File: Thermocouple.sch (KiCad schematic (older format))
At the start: 23 parts, among them P2 CONN_2, P3 CONN_3X2, U10 LMT84, U11 OPA4170, U9 MCP3901

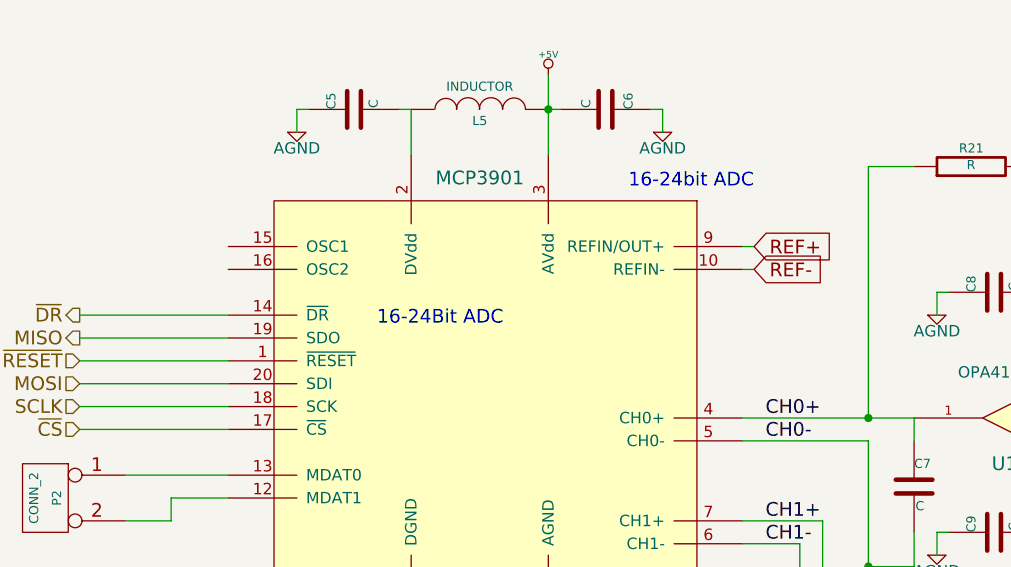
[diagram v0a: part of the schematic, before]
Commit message: Connected remaining ADC pins, some silk screen updates
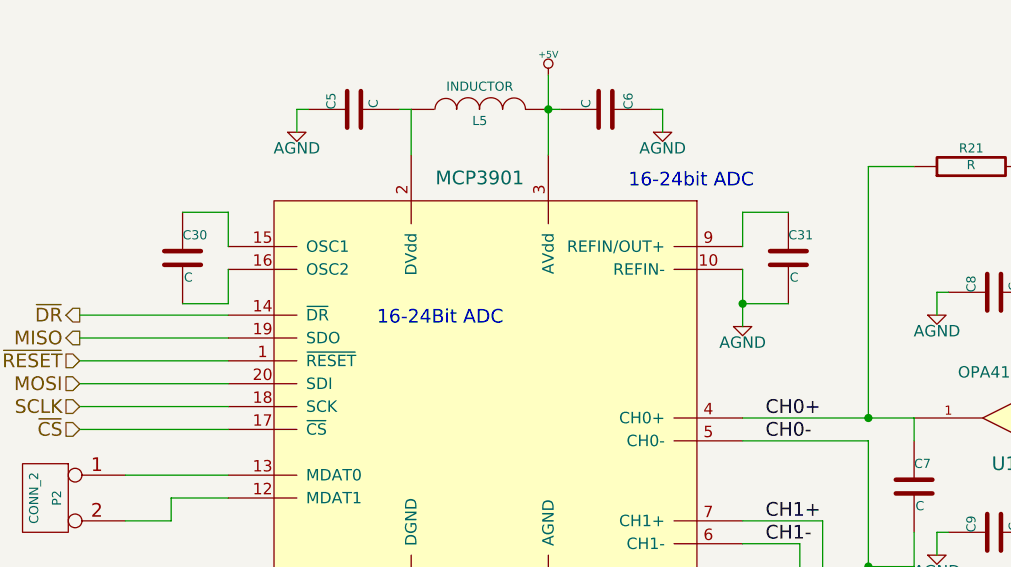
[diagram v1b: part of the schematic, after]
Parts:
- added C30, C31: C, symbol C
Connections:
- net REF- is gone; now on net AGND: U9.10 (REFIN-)
- net AGND: now also C31.2
- net at U9.15 (OSC1): now also C30.1
- net at U9.16 (OSC2): now also C30.2
- net REF+: no longer names the net of U9.9 (REFIN/OUT+)
- net REF+: now also C31.1
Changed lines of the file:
@@
 $EndComp
 $Comp
-L +5V #PWR60
+L +5V #PWR045
 U 1 1 530546E7
 P 5050 4750
-F 0 "#PWR60" H 5050 4840 20  0001 C CNN
+F 0 "#PWR045" H 5050 4840 20  0001 C CNN
 F 1 "+5V" H 5050 4840 30  0000 C CNN
 F 2 "" H 5050 4750 60  0000 C CNN
@@
 $EndComp
 $Comp
-L +5V #PWR53
+L +5V #PWR046
 U 1 1 53054B2C
 P 3100 1500
-F 0 "#PWR53" H 3100 1590 20  0001 C CNN
+F 0 "#PWR046" H 3100 1590 20  0001 C CNN
 F 1 "+5V" H 3100 1590 30  0000 C CNN
 F 2 "" H 3100 1500 60  0000 C CNN
@@
 	1    0    0    -1
 $EndComp
-Text GLabel 4000 2250 2    60   Input ~ 0
-REF+
-Text GLabel 4000 2350 2    60   Input ~ 0
-REF-
 $Comp
 L C C6
@@
 	3600 1650 3600 1750
 Wire Wire Line
-	4000 2350 3950 2350
-Wire Wire Line
-	4000 2250 3950 2250
-Wire Wire Line
 	3100 1500 3100 1850
 Connection ~ 5300 3500
@@
 	1050 3050 1700 3050
 $Comp
-L FE_V+ #PWR66
+L FE_V+ #PWR047
 U 1 1 530BD56D
 P 7800 4750
-F 0 "#PWR66" H 7800 4850 30  0001 C CNN
+F 0 "#PWR047" H 7800 4850 30  0001 C CNN
 F 1 "FE_V+" H 7800 4850 30  0000 C CNN
 F 2 "" H 7800 4750 60  0000 C CNN
@@
 $EndComp
 $Comp
-L FE_V+ #PWR62
+L FE_V+ #PWR048
 U 1 1 530BD573
 P 5300 3550
-F 0 "#PWR62" H 5300 3650 30  0001 C CNN
+F 0 "#PWR048" H 5300 3650 30  0001 C CNN
 F 1 "FE_V+" H 5300 3650 30  0000 C CNN
 F 2 "" H 5300 3550 60  0000 C CNN
@@
 $EndComp
 $Comp
-L FE_V+ #PWR63
+L FE_V+ #PWR049
 U 1 1 530BD635
 P 7800 1400
-F 0 "#PWR63" H 7800 1500 30  0001 C CNN
+F 0 "#PWR049" H 7800 1500 30  0001 C CNN
 F 1 "FE_V+" H 7800 1500 30  0000 C CNN
 F 2 "" H 7800 1400 60  0000 C CNN
@@
 Connection ~ 4200 6300
 $Comp
-L AGND #PWR51
+L AGND #PWR050
 U 1 1 531630FA
 P 2000 1750
-F 0 "#PWR51" H 2000 1750 40  0001 C CNN
+F 0 "#PWR050" H 2000 1750 40  0001 C CNN
 F 1 "AGND" H 2000 1680 50  0000 C CNN
 F 2 "" H 2000 1750 60  0000 C CNN
@@
 $EndComp
 $Comp
-L AGND #PWR55
+L AGND #PWR051
 U 1 1 53163116
 P 3600 1750
-F 0 "#PWR55" H 3600 1750 40  0001 C CNN
+F 0 "#PWR051" H 3600 1750 40  0001 C CNN
 F 1 "AGND" H 3600 1680 50  0000 C CNN
 F 2 "" H 3600 1750 60  0000 C CNN
@@
 $EndComp
 $Comp
-L AGND #PWR52
+L AGND #PWR052
 U 1 1 5316312B
 P 2500 4050
-F 0 "#PWR52" H 2500 4050 40  0001 C CNN
+F 0 "#PWR052" H 2500 4050 40  0001 C CNN
 F 1 "AGND" H 2500 3980 50  0000 C CNN
 F 2 "" H 2500 4050 60  0000 C CNN
@@
 $EndComp
 $Comp
-L AGND #PWR54
+L AGND #PWR053
 U 1 1 53163136
 P 3100 4050
-F 0 "#PWR54" H 3100 4050 40  0001 C CNN
+F 0 "#PWR053" H 3100 4050 40  0001 C CNN
 F 1 "AGND" H 3100 3980 50  0000 C CNN
 F 2 "" H 3100 4050 60  0000 C CNN
@@
 $EndComp
 $Comp
-L AGND #PWR56
+L AGND #PWR054
 U 1 1 53163155
 P 4200 6450
-F 0 "#PWR56" H 4200 6450 40  0001 C CNN
+F 0 "#PWR054" H 4200 6450 40  0001 C CNN
 F 1 "AGND" H 4200 6380 50  0000 C CNN
 F 2 "" H 4200 6450 60  0000 C CNN
@@
 $EndComp
 $Comp
-L AGND #PWR58
+L AGND #PWR055
 U 1 1 5316316A
 P 4800 2550
-F 0 "#PWR58" H 4800 2550 40  0001 C CNN
+F 0 "#PWR055" H 4800 2550 40  0001 C CNN
 F 1 "AGND" H 4800 2480 50  0000 C CNN
 F 2 "" H 4800 2550 60  0000 C CNN
@@
 $EndComp
 $Comp
-L AGND #PWR59
+L AGND #PWR056
 U 1 1 53163175
 P 4800 3600
-F 0 "#PWR59" H 4800 3600 40  0001 C CNN
+F 0 "#PWR056" H 4800 3600 40  0001 C CNN
 F 1 "AGND" H 4800 3530 50  0000 C CNN
 F 2 "" H 4800 3600 60  0000 C CNN
@@
 $EndComp
 $Comp
-L AGND #PWR57
+L AGND #PWR057
 U 1 1 531E51B9
 P 4500 4450
-F 0 "#PWR57" H 4500 4450 40  0001 C CNN
+F 0 "#PWR057" H 4500 4450 40  0001 C CNN
 F 1 "AGND" H 4500 4380 50  0000 C CNN
 F 2 "" H 4500 4450 60  0000 C CNN
@@
 Wire Wire Line
 	2500 1650 2500 1850
+$Comp
+L C C30
+U 1 1 5320C63A
+P 1500 2300
+F 0 "C30" H 1500 2400 40  0000 L CNN
+F 1 "C" H 1506 2215 40  0000 L CNN
+F 2 "" H 1538 2150 30  0000 C CNN
+F 3 "" H 1500 2300 60  0000 C CNN
+	1    1500 2300
+	1    0    0    -1
+$EndComp
+Wire Wire Line
+	1500 2100 1700 2100
+Wire Wire Line
+	1700 2100 1700 2250
+Wire Wire Line
+	1500 2500 1700 2500
+Wire Wire Line
+	1700 2500 1700 2350
+$Comp
+L C C31
+U 1 1 5320C72E
+P 4150 2300
+F 0 "C31" H 4150 2400 40  0000 L CNN
+F 1 "C" H 4156 2215 40  0000 L CNN
+F 2 "" H 4188 2150 30  0000 C CNN
+F 3 "" H 4150 2300 60  0000 C CNN
+	1    4150 2300
+	1    0    0    -1
+$EndComp
+Wire Wire Line
+	4150 2100 3950 2100
+Wire Wire Line
+	4150 2500 3950 2500
+Wire Wire Line
+	3950 2100 3950 2250
+Wire Wire Line
+	3950 2350 3950 2600
+$Comp
+L AGND #PWR058
+U 1 1 5320CB7D
+P 3950 2600
+F 0 "#PWR058" H 3950 2600 40  0001 C CNN
+F 1 "AGND" H 3950 2530 50  0000 C CNN
+F 2 "" H 3950 2600 60  0000 C CNN
+F 3 "" H 3950 2600 60  0000 C CNN
+	1    3950 2600
+	1    0    0    -1
+$EndComp
+Connection ~ 3950 2500
 $EndSCHEMATC

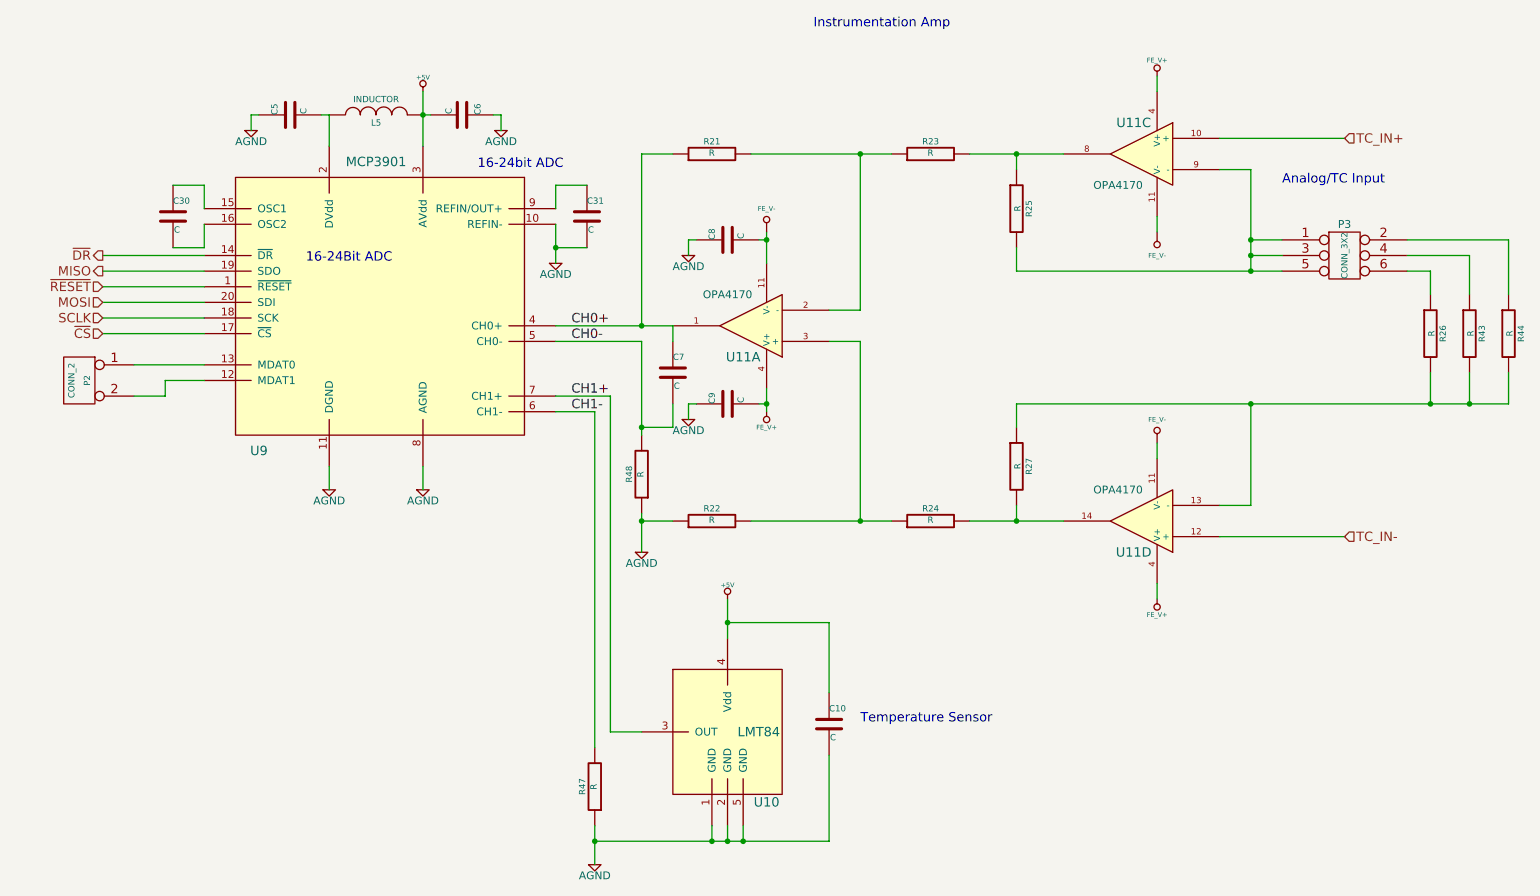
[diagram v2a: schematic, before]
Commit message: Test points added, silk screen updates
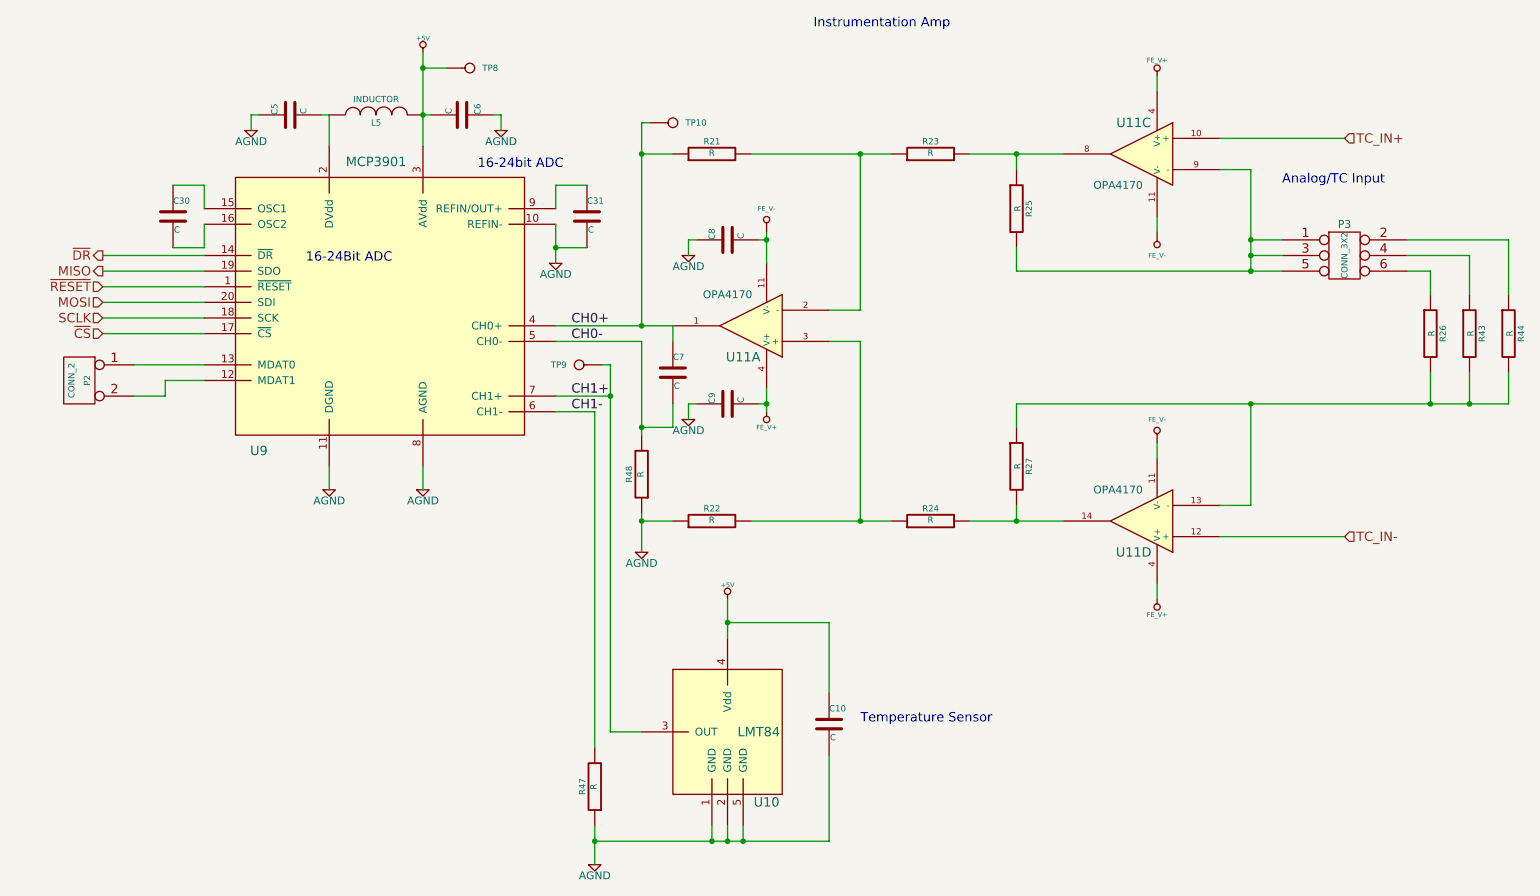
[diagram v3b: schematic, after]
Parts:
- added TP10: CH0+, symbol CONN_1
- added TP8: +5V, symbol CONN_1
- added TP9: CH1+, symbol CONN_1
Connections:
- net +5V: now also TP8.1
- net CH0+: now also TP10.1
- net CH1+: now also TP9.1
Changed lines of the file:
@@
 $EndComp
 $Comp
-L +5V #PWR63
+L +5V #PWR047
 U 1 1 530546E7
 P 5050 4750
-F 0 "#PWR63" H 5050 4840 20  0001 C CNN
+F 0 "#PWR047" H 5050 4840 20  0001 C CNN
 F 1 "+5V" H 5050 4840 30  0000 C CNN
 F 2 "" H 5050 4750 60  0000 C CNN
@@
 $EndComp
 $Comp
-L +5V #PWR55
+L +5V #PWR048
 U 1 1 53054B2C
-P 3100 1500
-F 0 "#PWR55" H 3100 1590 20  0001 C CNN
-F 1 "+5V" H 3100 1590 30  0000 C CNN
-F 2 "" H 3100 1500 60  0000 C CNN
-F 3 "" H 3100 1500 60  0000 C CNN
-	1    3100 1500
+P 3100 1250
+F 0 "#PWR048" H 3100 1340 20  0001 C CNN
+F 1 "+5V" H 3100 1340 30  0000 C CNN
+F 2 "" H 3100 1250 60  0000 C CNN
+F 3 "" H 3100 1250 60  0000 C CNN
+	1    3100 1250
 	1    0    0    -1
 $EndComp
@@
 $EndComp
 $Comp
-L FE_V+ #PWR69
+L FE_V+ #PWR049
 U 1 1 530BD56D
 P 7800 4750
-F 0 "#PWR69" H 7800 4850 30  0001 C CNN
+F 0 "#PWR049" H 7800 4850 30  0001 C CNN
 F 1 "FE_V+" H 7800 4850 30  0000 C CNN
 F 2 "" H 7800 4750 60  0000 C CNN
@@
 $EndComp
 $Comp
-L FE_V+ #PWR65
+L FE_V+ #PWR050
 U 1 1 530BD573
 P 5300 3550
-F 0 "#PWR65" H 5300 3650 30  0001 C CNN
+F 0 "#PWR050" H 5300 3650 30  0001 C CNN
 F 1 "FE_V+" H 5300 3650 30  0000 C CNN
 F 2 "" H 5300 3550 60  0000 C CNN
@@
 $EndComp
 $Comp
-L FE_V+ #PWR66
+L FE_V+ #PWR051
 U 1 1 530BD635
 P 7800 1400
-F 0 "#PWR66" H 7800 1500 30  0001 C CNN
+F 0 "#PWR051" H 7800 1500 30  0001 C CNN
 F 1 "FE_V+" H 7800 1500 30  0000 C CNN
 F 2 "" H 7800 1400 60  0000 C CNN
@@
 $EndComp
 $Comp
-L AGND #PWR53
+L AGND #PWR052
 U 1 1 531630FA
 P 2000 1750
-F 0 "#PWR53" H 2000 1750 40  0001 C CNN
+F 0 "#PWR052" H 2000 1750 40  0001 C CNN
 F 1 "AGND" H 2000 1680 50  0000 C CNN
 F 2 "" H 2000 1750 60  0000 C CNN
@@
 $EndComp
 $Comp
-L AGND #PWR57
+L AGND #PWR053
 U 1 1 53163116
 P 3600 1750
-F 0 "#PWR57" H 3600 1750 40  0001 C CNN
+F 0 "#PWR053" H 3600 1750 40  0001 C CNN
 F 1 "AGND" H 3600 1680 50  0000 C CNN
 F 2 "" H 3600 1750 60  0000 C CNN
@@
 $EndComp
 $Comp
-L AGND #PWR54
+L AGND #PWR054
 U 1 1 5316312B
 P 2500 4050
-F 0 "#PWR54" H 2500 4050 40  0001 C CNN
+F 0 "#PWR054" H 2500 4050 40  0001 C CNN
 F 1 "AGND" H 2500 3980 50  0000 C CNN
 F 2 "" H 2500 4050 60  0000 C CNN
@@
 $EndComp
 $Comp
-L AGND #PWR56
+L AGND #PWR055
 U 1 1 53163136
 P 3100 4050
-F 0 "#PWR56" H 3100 4050 40  0001 C CNN
+F 0 "#PWR055" H 3100 4050 40  0001 C CNN
 F 1 "AGND" H 3100 3980 50  0000 C CNN
 F 2 "" H 3100 4050 60  0000 C CNN
@@
 $EndComp
 $Comp
-L AGND #PWR59
+L AGND #PWR056
 U 1 1 53163155
 P 4200 6450
-F 0 "#PWR59" H 4200 6450 40  0001 C CNN
+F 0 "#PWR056" H 4200 6450 40  0001 C CNN
 F 1 "AGND" H 4200 6380 50  0000 C CNN
 F 2 "" H 4200 6450 60  0000 C CNN
@@
 $EndComp
 $Comp
-L AGND #PWR61
+L AGND #PWR057
 U 1 1 5316316A
 P 4800 2550
-F 0 "#PWR61" H 4800 2550 40  0001 C CNN
+F 0 "#PWR057" H 4800 2550 40  0001 C CNN
 F 1 "AGND" H 4800 2480 50  0000 C CNN
 F 2 "" H 4800 2550 60  0000 C CNN
@@
 $EndComp
 $Comp
-L AGND #PWR62
+L AGND #PWR058
 U 1 1 53163175
 P 4800 3600
-F 0 "#PWR62" H 4800 3600 40  0001 C CNN
+F 0 "#PWR058" H 4800 3600 40  0001 C CNN
 F 1 "AGND" H 4800 3530 50  0000 C CNN
 F 2 "" H 4800 3600 60  0000 C CNN
@@
 $EndComp
 $Comp
-L AGND #PWR60
+L AGND #PWR059
 U 1 1 531E51B9
 P 4500 4450
-F 0 "#PWR60" H 4500 4450 40  0001 C CNN
+F 0 "#PWR059" H 4500 4450 40  0001 C CNN
 F 1 "AGND" H 4500 4380 50  0000 C CNN
 F 2 "" H 4500 4450 60  0000 C CNN
@@
 $EndComp
 $Comp
-L AGND #PWR58
+L AGND #PWR060
 U 1 1 5320CB7D
 P 3950 2600
-F 0 "#PWR58" H 3950 2600 40  0001 C CNN
+F 0 "#PWR060" H 3950 2600 40  0001 C CNN
 F 1 "AGND" H 3950 2530 50  0000 C CNN
 F 2 "" H 3950 2600 60  0000 C CNN
@@
 	8200 2000 8400 2000
 Wire Wire Line
-	10050 3500 6900 3500
+	6900 3500 10050 3500
 Wire Wire Line
 	8400 4150 8400 3500
@@
 	8200 4150 8400 4150
 Wire Wire Line
-	4500 1900 4500 3000
+	4500 1700 4500 3000
 Wire Wire Line
 	5900 2900 5900 1900
@@
 Connection ~ 9550 3500
 Wire Wire Line
-	10050 3300 10050 3500
+	10050 3500 10050 3300
 Connection ~ 9800 3500
 Wire Wire Line
@@
 	3950 3450 4300 3450
 Wire Wire Line
-	4300 3450 4300 5600
+	4300 3250 4300 5600
 Wire Wire Line
 	4300 5600 4500 5600
@@
 Connection ~ 5300 3500
 Wire Wire Line
-	3100 1500 3100 1850
+	3100 1250 3100 1850
 Wire Wire Line
 	3600 1650 3600 1750
@@
 Wire Wire Line
 	4200 3550 4200 5700
+$Comp
+L CONN_1 TP10
+U 1 1 53223FBC
+P 4700 1700
+F 0 "TP10" H 4780 1700 40  0000 L CNN
+F 1 "CH0+" H 4700 1755 30  0001 C CNN
+F 2 "" H 4700 1700 60  0000 C CNN
+F 3 "" H 4700 1700 60  0000 C CNN
+	1    4700 1700
+	1    0    0    -1
+$EndComp
+Wire Wire Line
+	4500 1700 4550 1700
+Connection ~ 4500 1900
+$Comp
+L CONN_1 TP9
+U 1 1 53224064
+P 4100 3250
+F 0 "TP9" H 4180 3250 40  0000 L CNN
+F 1 "CH1+" H 4100 3305 30  0001 C CNN
+F 2 "" H 4100 3250 60  0000 C CNN
+F 3 "" H 4100 3250 60  0000 C CNN
+	1    4100 3250
+	-1   0    0    1
+$EndComp
+Connection ~ 4300 3450
+Wire Wire Line
+	4300 3250 4250 3250
+$Comp
+L CONN_1 TP8
+U 1 1 53225571
+P 3400 1350
+F 0 "TP8" H 3480 1350 40  0000 L CNN
+F 1 "+5V" H 3400 1405 30  0001 C CNN
+F 2 "" H 3400 1350 60  0000 C CNN
+F 3 "" H 3400 1350 60  0000 C CNN
+	1    3400 1350
+	1    0    0    -1
+$EndComp
+Wire Wire Line
+	3250 1350 3100 1350
+Connection ~ 3100 1350
 $EndSCHEMATC
